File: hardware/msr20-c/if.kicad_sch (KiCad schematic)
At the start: 0 parts

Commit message: add bpf and fixed-gain amp to if stage
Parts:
- added C10, C4: 1.2n, symbol Device:C
- added C11, C12, C13, C14, C15: 100n, symbol Device:C
- added L2, L3: 92m, symbol Device:L
- added L4: 10m, symbol Device:L
- added Q3, Q4: NPN, symbol Simulation_SPICE:NPN
- added R10: 470, symbol Device:R
- added R5: 6.8k, symbol Device:R
- added R6: 3.3k, symbol Device:R
- added R7: 200, symbol Device:R
- added R8: 10k, symbol Device:R
- added R9: 47, symbol Device:R
- added U3: LTC455-FU, msr20:LTC455, symbol msr20:LTC455-FU
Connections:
- new net: C12.2, L2.1
- new net: C4.1, L2.2, U3.1 (IN)
- new net: C11.1, L3.2
- new net: C11.2, Q3.2 (B), R5.2, R6.1
- new net: C13.1, L4.1, R8.1, R9.2
- new net: C10.1, L3.1, U3.2 (OUT)
- new net: L4.2, Q3.1 (C), Q4.2 (B), R8.2
- new net: C15.2, Q3.3 (E), R7.1
- new net: C14.1, Q4.3 (E), R10.1
- new net +5V: Q4.1 (C), R5.1, R9.1
- new net GND: C10.2, C13.2, C15.1, C4.2, R10.2, R6.2, R7.2, U3.3 (GND)
- new net IN: C12.1
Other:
- note added: "IF Amplifier (Stage 1)"
- note added: "IF Band-Pass Filter"

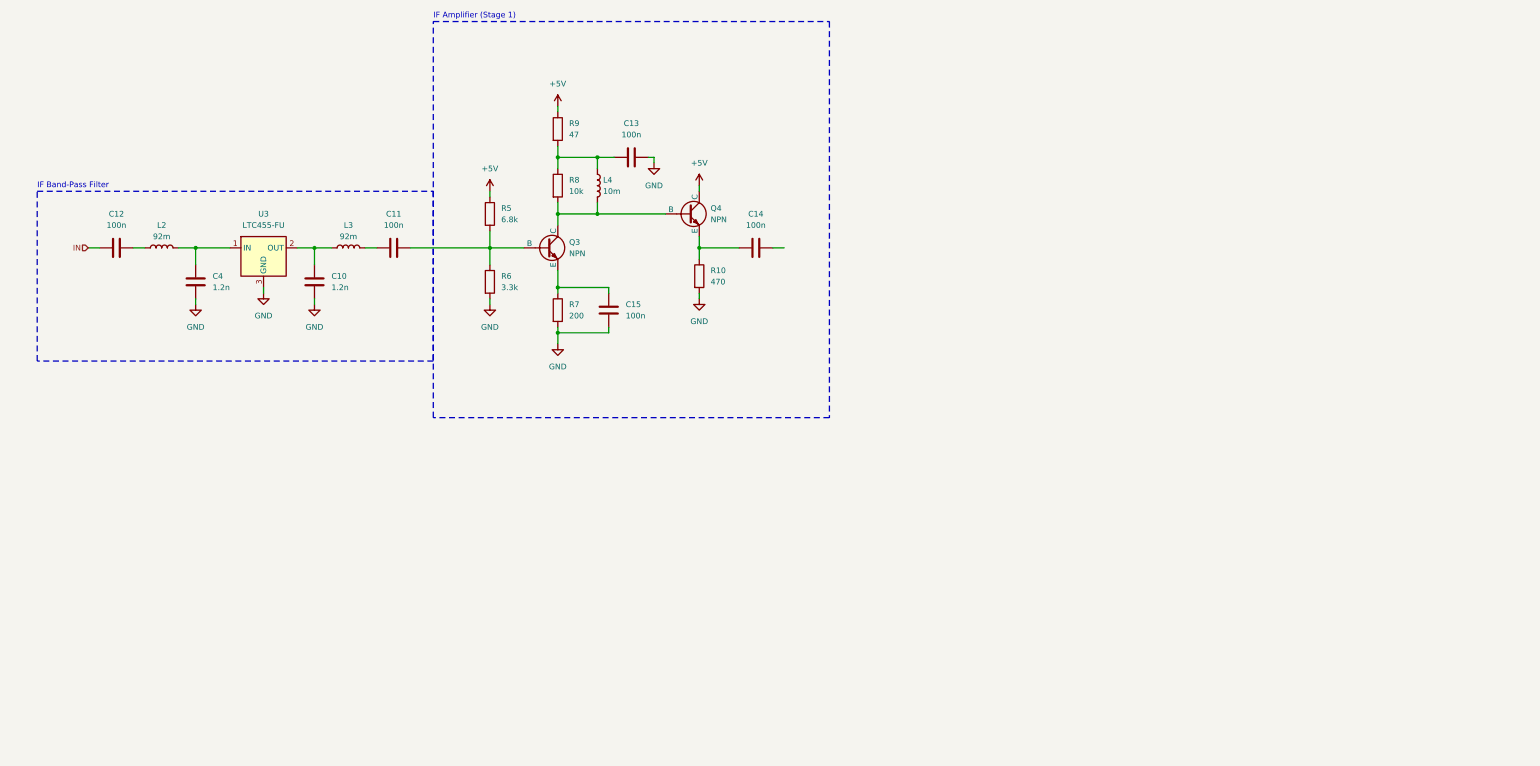
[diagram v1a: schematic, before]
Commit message: add stage 2 amp and adc to if schematic
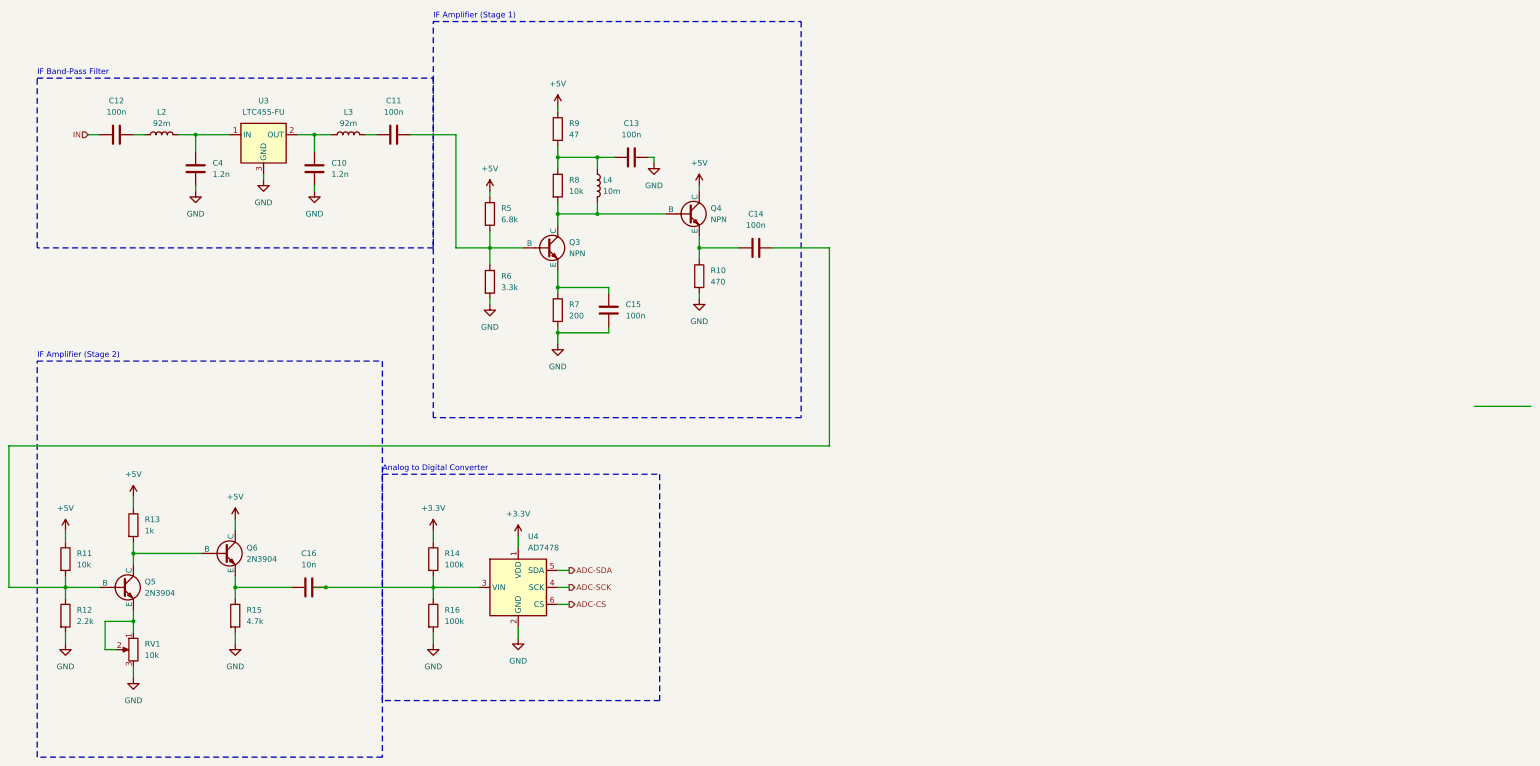
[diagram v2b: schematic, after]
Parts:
- added C16: 10n, symbol Device:C
- added Q5, Q6: 2N3904, symbol Simulation_SPICE:NPN
- added R11: 10k, symbol Device:R
- added R12: 2.2k, symbol Device:R
- added R13: 1k, symbol Device:R
- added R14, R16: 100k, symbol Device:R
- added R15: 4.7k, symbol Device:R
- added RV1: 10k, symbol Device:R_Potentiometer
- added U4: AD7478, Package_TO_SOT_SMD:SOT-23-6, symbol msr20:AD7478
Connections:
- net +5V: now also Q6.1 (C), R11.1, R13.1
- net GND: now also R12.2, R15.2, R16.2, RV1.3, U4.2 (GND)
- net at C14.2: now also Q5.2 (B), R11.2, R12.1
- new net: Q5.1 (C), Q6.2 (B), R13.2
- new net: Q5.3 (E), RV1.1, RV1.2
- new net: C16.1, Q6.3 (E), R15.1
- new net: C16.2, R14.2, R16.1, U4.3 (VIN)
- new net +3.3V: R14.1, U4.1 (VDD)
- new net ADC-CS: U4.6 (CS)
- new net ADC-SCK: U4.4 (SCK)
- new net ADC-SDA: U4.5 (SDA)
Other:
- note added: "Analog to Digital Converter"
- note added: "IF Amplifier (Stage 2)"
- moved on the sheet: C10, C11, C12, C4, L2, L3, U3

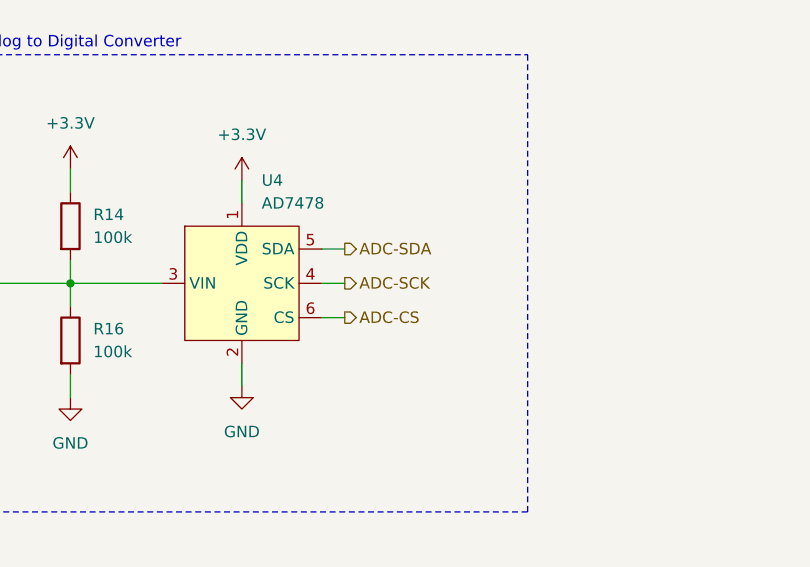
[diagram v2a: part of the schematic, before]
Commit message: add pico to schematic
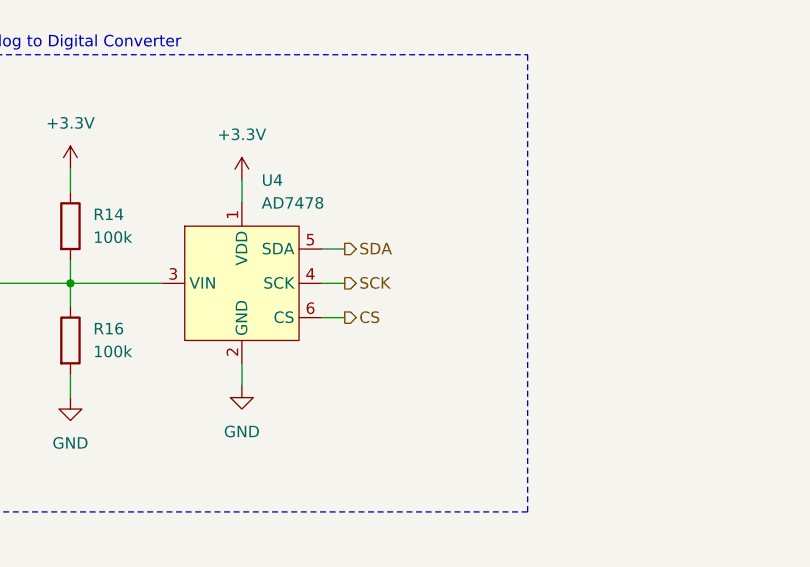
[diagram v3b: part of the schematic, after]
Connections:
- net ADC-CS renamed CS
- net ADC-SCK renamed SCK
- net ADC-SDA renamed SDA
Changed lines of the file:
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@@
 		)
 	)
-	(hierarchical_label "ADC-SCK"
+	(hierarchical_label "SCK"
 		(shape output)
 		(at 144.78 152.4 0)
@@
 		)
 	)
-	(hierarchical_label "ADC-CS"
+	(hierarchical_label "CS"
 		(shape output)
 		(at 144.78 156.21 0)
@@
 		)
 	)
-	(hierarchical_label "ADC-SDA"
+	(hierarchical_label "SDA"
 		(shape output)
 		(at 144.78 148.59 0)

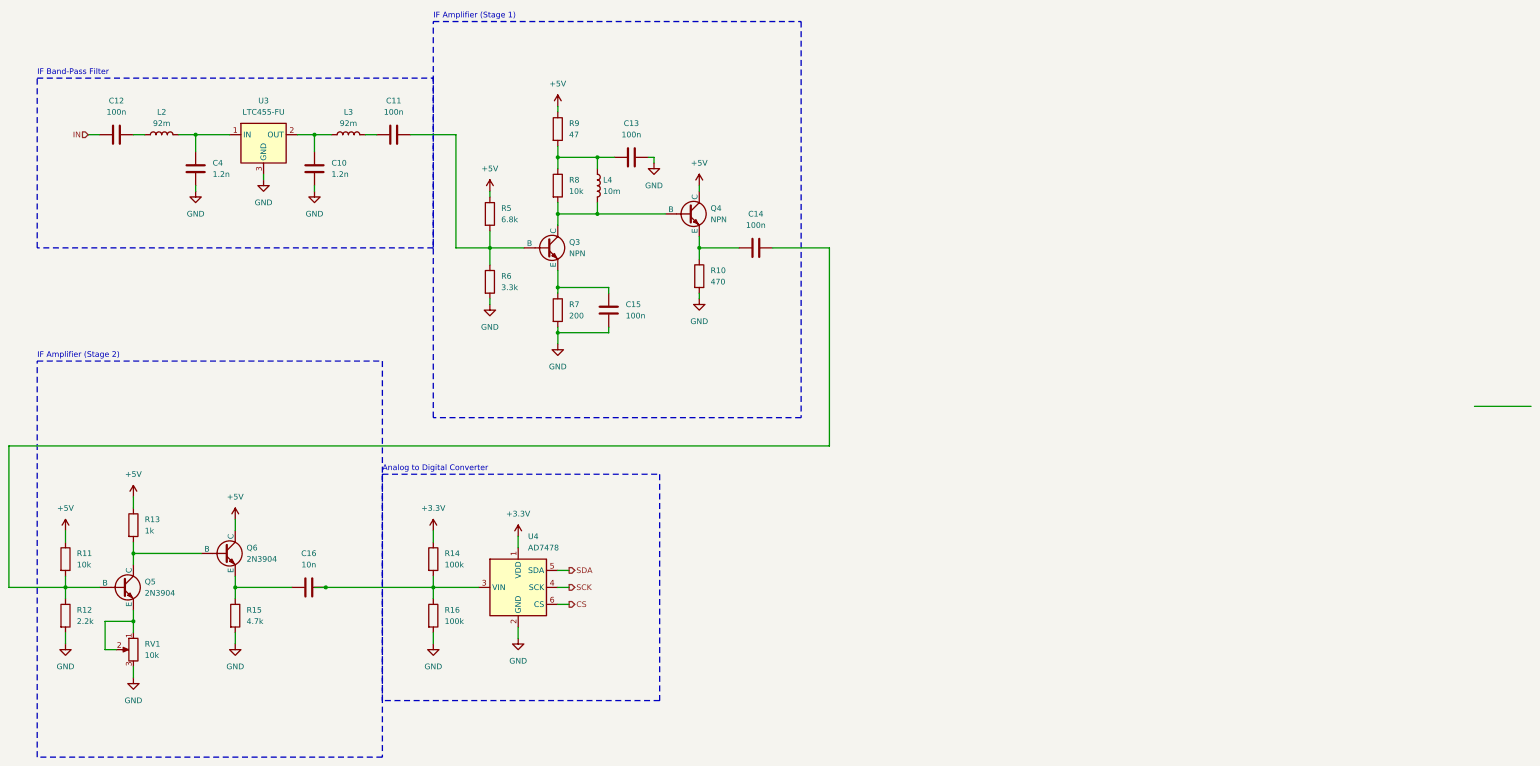
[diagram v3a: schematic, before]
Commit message: add power sheet, assign footprints
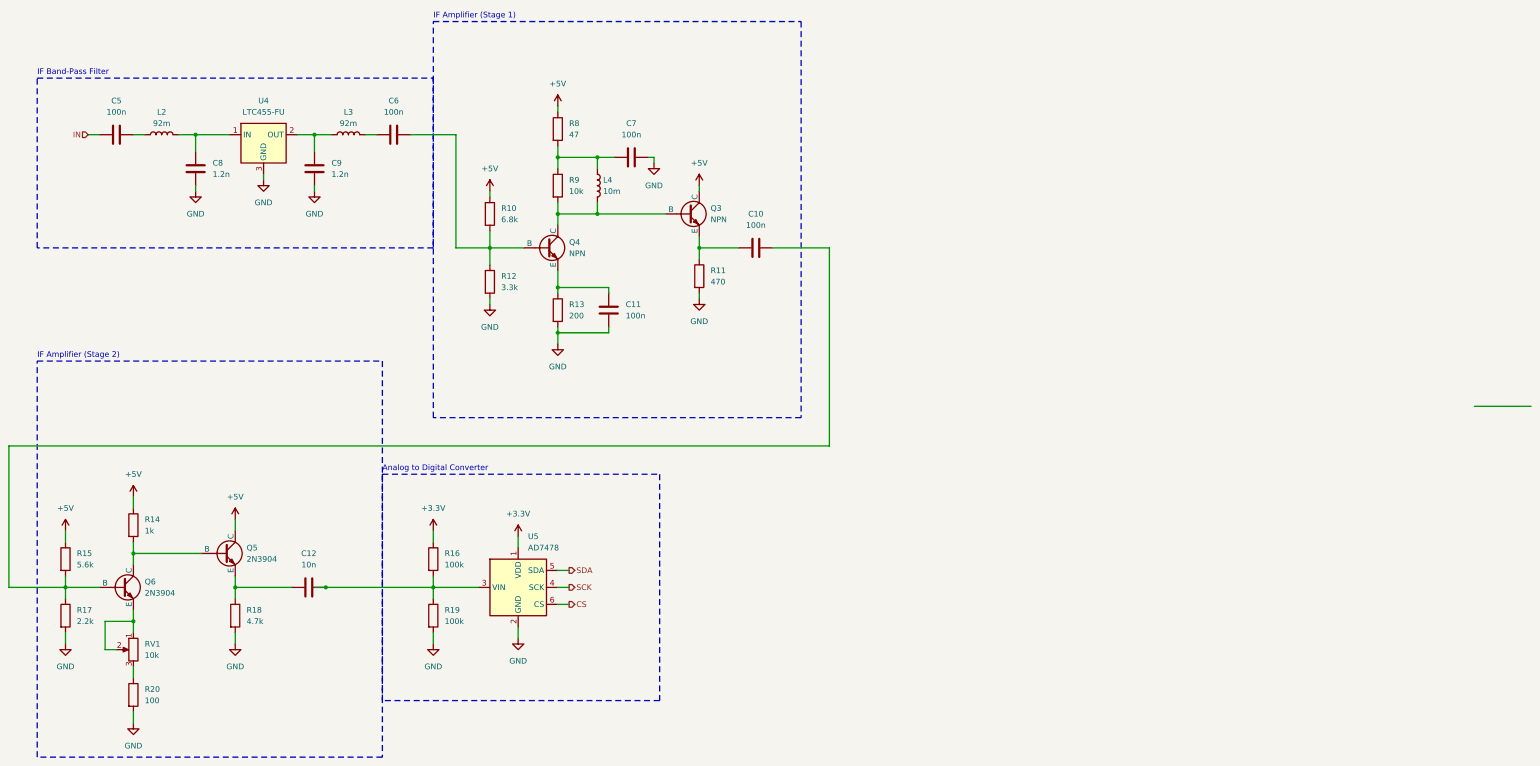
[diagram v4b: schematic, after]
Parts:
- added R20: 100, Resistor_SMD:R_0805_2012Metric, symbol Device:R
- C10: renamed from C14; footprint (none) -> Capacitor_SMD:C_0805_2012Metric
- C11: renamed from C15; footprint (none) -> Capacitor_SMD:C_0805_2012Metric
- C12: renamed from C16; footprint (none) -> Capacitor_SMD:C_0805_2012Metric
- C5: renamed from C12; footprint (none) -> Capacitor_SMD:C_0805_2012Metric
- C6: renamed from C11; footprint (none) -> Capacitor_SMD:C_0805_2012Metric
- C7: renamed from C13; footprint (none) -> Capacitor_SMD:C_0805_2012Metric
- C8: renamed from C4; footprint (none) -> Capacitor_SMD:C_0805_2012Metric
- C9: renamed from C10; footprint (none) -> Capacitor_SMD:C_0805_2012Metric
- L2, L3, L4: footprint (none) -> Inductor_SMD:L_0805_2012Metric
- Q3: renamed from Q4; footprint (none) -> Package_TO_SOT_THT:TO-92
- Q4: renamed from Q3; footprint (none) -> Package_TO_SOT_THT:TO-92
- Q5: renamed from Q6; footprint (none) -> Package_TO_SOT_THT:TO-92
- Q6: renamed from Q5; footprint (none) -> Package_TO_SOT_THT:TO-92
- R10: renamed from R5; footprint (none) -> Resistor_SMD:R_0805_2012Metric
- R11: renamed from R10; footprint (none) -> Resistor_SMD:R_0805_2012Metric
- R12: renamed from R6; footprint (none) -> Resistor_SMD:R_0805_2012Metric
- R13: renamed from R7; footprint (none) -> Resistor_SMD:R_0805_2012Metric
- R14: renamed from R13; footprint (none) -> Resistor_SMD:R_0805_2012Metric
- R15: renamed from R11; value 10k -> 5.6k; footprint (none) -> Resistor_SMD:R_0805_2012Metric
- R16: renamed from R14; footprint (none) -> Resistor_SMD:R_0805_2012Metric
- R17: renamed from R12; footprint (none) -> Resistor_SMD:R_0805_2012Metric
- R18: renamed from R15; footprint (none) -> Resistor_SMD:R_0805_2012Metric
- R19: renamed from R16; footprint (none) -> Resistor_SMD:R_0805_2012Metric
- R8: renamed from R9; footprint (none) -> Resistor_SMD:R_0805_2012Metric
- R9: renamed from R8; footprint (none) -> Resistor_SMD:R_0805_2012Metric
- RV1: footprint (none) -> Resistor_SMD:R_0805_2012Metric
- renumbered U3 to U4, U4 to U5
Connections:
- net GND: now also R20.2; no longer RV1.3
- new net: R20.1, RV1.3

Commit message: finish pcb rev 1, new png render
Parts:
- added TP3, TP4, TP5: TestPoint, TestPoint:TestPoint_Pad_D1.0mm, symbol Connector:TestPoint
- RV1: footprint Resistor_SMD:R_0805_2012Metric -> Connector_PinHeader_2.54mm:PinHeader_1x03_P2.54mm_Vertical
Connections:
- net at C10.2, Q6.2 (B), R15.2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: now also TP4.1
- net at C6.2, Q4.2 (B), R10.2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: now also TP3.1
- net at C12.2, R16.2, R19.1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: now also TP5.1
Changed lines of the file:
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@@
 	)
 	(junction
-		(at 127 76.2)
+		(at 203.2 76.2)
 		(diameter 0)
 		(color 0 0 0 0)
 	)
 	(junction
-		(at 142.24 95.25)
+		(at 119.38 50.8)
 		(diameter 0)
 		(color 0 0 0 0)
 	)
 	(junction
-		(at 31.75 152.4)
+		(at 95.25 152.4)
 		(diameter 0)
 		(color 0 0 0 0)
 	)
 	(junction
-		(at 69.85 152.4)
+		(at 127 76.2)
+		(diameter 0)
+		(color 0 0 0 0)
+	)
+	(junction
+		(at 142.24 95.25)
+		(diameter 0)
+		(color 0 0 0 0)
+	)
+	(junction
+		(at 31.75 152.4)
 		(diameter 0)
 		(color 0 0 0 0)
 	)
 	(junction
-		(at 90.17 152.4)
+		(at 69.85 152.4)
 		(diameter 0)
 		(color 0 0 0 0)
@@
 	(wire
 		(pts
-			(xy 46.99 144.78) (xy 62.23 144.78)
+			(xy 95.25 152.4) (xy 114.3 152.4)
 		)
 		(stroke
@@
 	(wire
 		(pts
-			(xy 142.24 152.4) (xy 144.78 152.4)
+			(xy 46.99 144.78) (xy 62.23 144.78)
 		)
 		(stroke
@@
 	(wire
 		(pts
-			(xy 87.63 152.4) (xy 90.17 152.4)
+			(xy 142.24 152.4) (xy 144.78 152.4)
 		)
 		(stroke
@@
 	(wire
 		(pts
-			(xy 90.17 152.4) (xy 114.3 152.4)
+			(xy 90.17 152.4) (xy 95.25 152.4)
 		)
 		(stroke
@@
 	(wire
 		(pts
+			(xy 95.25 148.59) (xy 95.25 152.4)
+		)
+		(stroke
+			(width 0)
+			(type default)
+		)
+	)
+	(wire
+		(pts
 			(xy 173.99 76.2) (xy 173.99 78.74)
 		)
@@
 	(wire
 		(pts
+			(xy 119.38 50.8) (xy 123.19 50.8)
+		)
+		(stroke
+			(width 0)
+			(type default)
+		)
+	)
+	(wire
+		(pts
 			(xy 19.05 152.4) (xy 31.75 152.4)
 		)
@@
 	(wire
 		(pts
+			(xy 203.2 73.66) (xy 203.2 76.2)
+		)
+		(stroke
+			(width 0)
+			(type default)
+		)
+	)
+	(wire
+		(pts
 			(xy 31.75 139.7) (xy 31.75 142.24)
 		)
@@
 	)
 	(symbol
+		(lib_id "Connector:TestPoint")
+		(at 95.25 148.59 0)
+		(unit 1)
+		(exclude_from_sim no)
+		(in_bom yes)
+		(on_board yes)
+		(dnp no)
+		(fields_autoplaced yes)
+		(property "Reference" "TP5"
+			(at 97.79 144.0179 0)
+			(effects
+				(font
+					(size 1.27 1.27)
+				)
+				(justify left)
+			)
+		)
+		(property "Value" "TestPoint"
+			(at 97.79 146.5579 0)
+			(effects
+				(font
+					(size 1.27 1.27)
+				)
+				(justify left)
+			)
+		)
+		(property "Footprint" "TestPoint:TestPoint_Pad_D1.0mm"
+			(at 100.33 148.59 0)
+			(effects
+				(font
+					(size 1.27 1.27)
+				)
+				(hide yes)
+			)
+		)
+		(property "Datasheet" "~"
+			(at 100.33 148.59 0)
+			(effects
+				(font
+					(size 1.27 1.27)
+				)
+				(hide yes)
+			)
+		)
+		(property "Description" "test point"
+			(at 95.25 148.59 0)
+			(effects
+				(font
+					(size 1.27 1.27)
+				)
+				(hide yes)
+			)
+		)
+		(pin "1"
+		)
+		(instances
+			(project "msr20-c"
+				(path "/3d24e86e-b070-4f0e-8c28-04e9dd9d95d1/841913b6-5fbe-4f9b-b6b5-daa29caf24de"
+					(reference "TP5")
+					(unit 1)
+				)
+			)
+		)
+	)
+	(symbol
 		(lib_id "power:+3.3V")
 		(at 114.3 139.7 0)
@@
 	)
 	(symbol
+		(lib_id "Connector:TestPoint")
+		(at 203.2 73.66 0)
+		(unit 1)
+		(exclude_from_sim no)
+		(in_bom yes)
+		(on_board yes)
+		(dnp no)
+		(fields_autoplaced yes)
+		(property "Reference" "TP4"
+			(at 205.74 69.0879 0)
+			(effects
+				(font
+					(size 1.27 1.27)
+				)
+				(justify left)
+			)
+		)
+		(property "Value" "TestPoint"
+			(at 205.74 71.6279 0)
+			(effects
+				(font
+					(size 1.27 1.27)
+				)
+				(justify left)
+			)
+		)
+		(property "Footprint" "TestPoint:TestPoint_Pad_D1.0mm"
+			(at 208.28 73.66 0)
+			(effects
+				(font
+					(size 1.27 1.27)
+				)
+				(hide yes)
+			)
+		)
+		(property "Datasheet" "~"
+			(at 208.28 73.66 0)
+			(effects
+				(font
+					(size 1.27 1.27)
+				)
+				(hide yes)
+			)
+		)
+		(property "Description" "test point"
+			(at 203.2 73.66 0)
+			(effects
+				(font
+					(size 1.27 1.27)
+				)
+				(hide yes)
+			)
+		)
+		(pin "1"
+		)
+		(instances
+			(project "msr20-c"
+				(path "/3d24e86e-b070-4f0e-8c28-04e9dd9d95d1/841913b6-5fbe-4f9b-b6b5-daa29caf24de"
+					(reference "TP4")
+					(unit 1)
+				)
+			)
+		)
+	)
+	(symbol
 		(lib_id "power:GND")
 		(at 31.75 165.1 0)
@@
 	)
 	(symbol
+		(lib_id "Connector:TestPoint")
+		(at 123.19 50.8 270)
+		(unit 1)
+		(exclude_from_sim no)
+		(in_bom yes)
+		(on_board yes)
+		(dnp no)
+		(fields_autoplaced yes)
+		(property "Reference" "TP3"
+			(at 128.27 49.5299 90)
+			(effects
+				(font
+					(size 1.27 1.27)
+				)
+				(justify left)
+			)
+		)
+		(property "Value" "TestPoint"
+			(at 128.27 52.0699 90)
+			(effects
+				(font
+					(size 1.27 1.27)
+				)
+				(justify left)
+			)
+		)
+		(property "Footprint" "TestPoint:TestPoint_Pad_D1.0mm"
+			(at 123.19 55.88 0)
+			(effects
+				(font
+					(size 1.27 1.27)
+				)
+				(hide yes)
+			)
+		)
+		(property "Datasheet" "~"
+			(at 123.19 55.88 0)
+			(effects
+				(font
+					(size 1.27 1.27)
+				)
+				(hide yes)
+			)
+		)
+		(property "Description" "test point"
+			(at 123.19 50.8 0)
+			(effects
+				(font
+					(size 1.27 1.27)
+				)
+				(hide yes)
+			)
+		)
+		(pin "1"
+		)
+		(instances
+			(project "msr20-c"
+				(path "/3d24e86e-b070-4f0e-8c28-04e9dd9d95d1/841913b6-5fbe-4f9b-b6b5-daa29caf24de"
+					(reference "TP3")
+					(unit 1)
+				)
+			)
+		)
+	)
+	(symbol
 		(lib_id "Device:L")
 		(at 95.25 50.8 90)
@@
 			)
 		)
-		(property "Footprint" "Resistor_SMD:R_0805_2012Metric"
+		(property "Footprint" "Connector_PinHeader_2.54mm:PinHeader_1x03_P2.54mm_Vertical"
 			(at 46.99 166.37 0)
 			(effects

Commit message: plot msr20-c schematic and pcb
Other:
- title: (none) -> IF Stage
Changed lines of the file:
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@@
 	(generator "eeschema")
 	(generator_version "8.0")
-	(paper "A4")
+	(paper "USLetter")
+	(title_block
+		(title "IF Stage")
+		(date "2024-04-29")
+		(rev "1")
+	)
 	(junction
 		(at 60.96 50.8)
